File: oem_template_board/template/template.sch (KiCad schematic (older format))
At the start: 28 parts, among them J1 CONN_02X03, U1 MCP2561-E_SN, U101 TPS560430YF, U2 ATMEGA16M1, Y1 Crystal_SMD

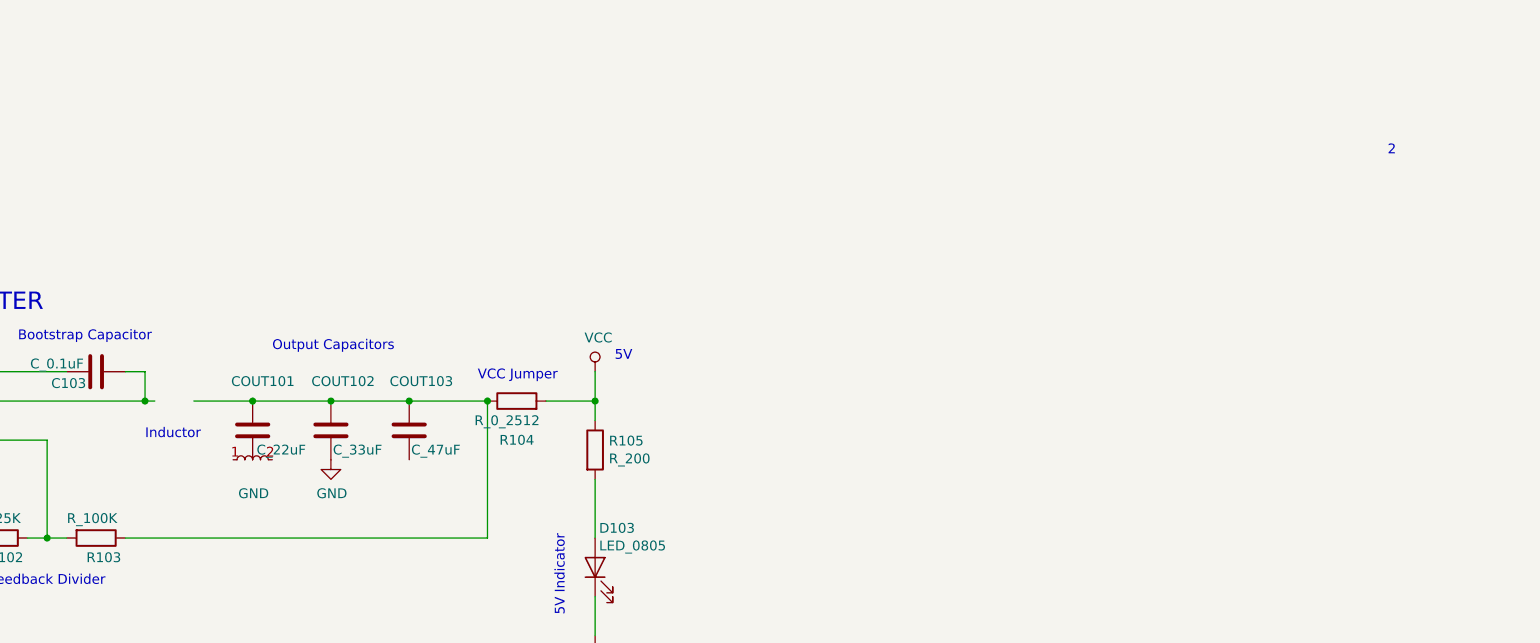
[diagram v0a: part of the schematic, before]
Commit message: fix inductor and bypass cap connections
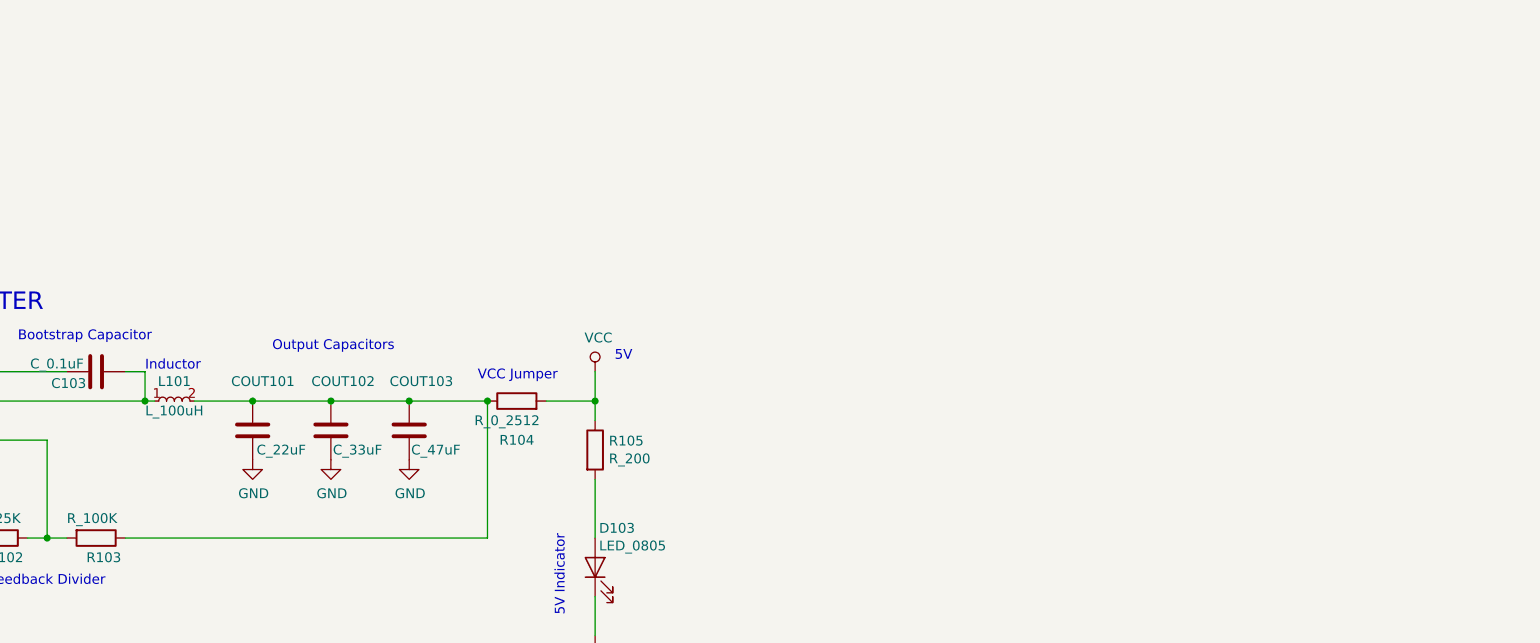
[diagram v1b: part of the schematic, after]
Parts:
- added L101: L_100uH, formula:L_100uH, symbol template-rescue:L_100uH-formula
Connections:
- net GND: now also COUT101.2, COUT103.2
- net at C103.2, U101.6 (SW): now also L101.1
- net at COUT101.1, COUT102.1, COUT103.1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: now also L101.2
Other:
- note removed: "2"
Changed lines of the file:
@@
 Text Notes 3450 9850 0    50   ~ 0
 Feedback Divider\n
-Text Notes 4250 9100 0    50   ~ 0
-Inductor\n
 Text Notes 3600 8600 0    50   ~ 0
 Bootstrap Capacitor\n
 Text Notes 4900 8650 0    50   ~ 0
 Output Capacitors\n
-$Comp
-L template-rescue:L_100uH-formula #PWR0109
-U 1 1 5C781579
-P 4800 9200
-F 0 "#PWR0109" H 4800 8950 50  0001 C CNN
-F 1 "GND" H 4805 9027 50  0000 C CNN
-F 2 "" H 4800 9200 50  0001 C CNN
-F 3 "" H 4800 9200 50  0001 C CNN
-F 4 "Digikey" H 4900 9000 50  0001 C CNN "MFN"
-F 5 "445-15759-1-ND" H 4800 9450 50  0001 C CNN "MPN"
-F 6 "https://www.digikey.com/product-detail/en/tdk-corporation/NLFV32T-101K-EF/445-15759-1-ND/4328055" H 5100 9400 50  0001 C CNN "Link"
-	1    4800 9200
-	1    0    0    -1
-$EndComp
 $Comp
 L power:GND #PWR0110
@@
 Text Notes 6400 10000 1    50   ~ 0
 5V Indicator
-Text Notes 10600 7650 0    50   ~ 0
-2
 $Comp
 L template-rescue:ATMEGA16M1-formula U2
@@
 	1700 8800 2100 8800
 Connection ~ 1700 8800
+Text Notes 4250 8750 0    50   ~ 0
+Inductor\n
+$Comp
+L power:GND #PWR?
+U 1 1 5F87F709
+P 4800 9200
+F 0 "#PWR?" H 4800 8950 50  0001 C CNN
+F 1 "GND" H 4805 9027 50  0000 C CNN
+F 2 "" H 4800 9200 50  0001 C CNN
+F 3 "" H 4800 9200 50  0001 C CNN
+	1    4800 9200
+	1    0    0    -1
+$EndComp
+$Comp
+L power:GND #PWR?
+U 1 1 5F87F995
+P 5600 9200
+F 0 "#PWR?" H 5600 8950 50  0001 C CNN
+F 1 "GND" H 5605 9027 50  0000 C CNN
+F 2 "" H 5600 9200 50  0001 C CNN
+F 3 "" H 5600 9200 50  0001 C CNN
+	1    5600 9200
+	1    0    0    -1
+$EndComp
+$Comp
+L template-rescue:L_100uH-formula L101
+U 1 1 5F881F17
+P 4400 8900
+F 0 "L101" H 4400 9000 50  0000 C CNN
+F 1 "L_100uH" H 4400 8850 50  0000 C CNN
+F 2 "formula:L_100uH" H 4300 8700 50  0001 C CNN
+F 3 "https://product.tdk.com/info/en/catalog/datasheets/inductor_commercial_decoupling_nlfv32-ef_en.pdf" H 4300 8750 50  0001 C CNN
+F 4 "Digikey" H 4500 8700 50  0001 C CNN "MFN"
+F 5 "445-15759-1-ND" H 4400 9150 50  0001 C CNN "MPN"
+F 6 "https://www.digikey.com/product-detail/en/tdk-corporation/NLFV32T-101K-EF/445-15759-1-ND/4328055" H 4700 9100 50  0001 C CNN "Link"
+	1    4400 8900
+	1    0    0    -1
+$EndComp
 $EndSCHEMATC

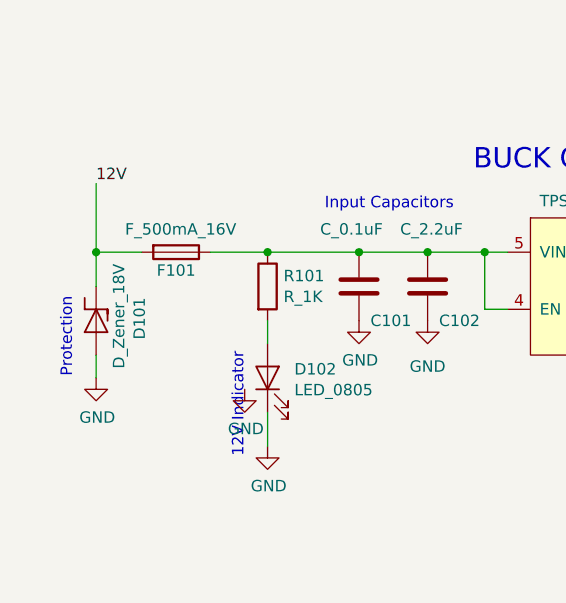
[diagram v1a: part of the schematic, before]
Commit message: move fuse before zener diode so it pops during an over-voltage event
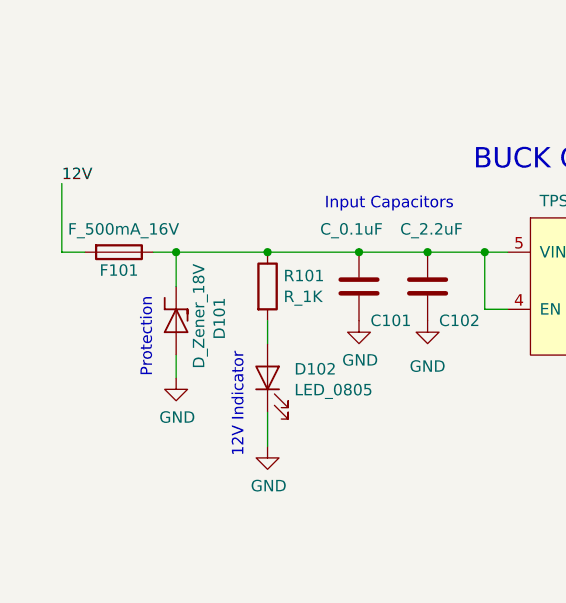
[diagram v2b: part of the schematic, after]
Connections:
- net 12V: no longer D101.1 (K)
- net at C101.1, C102.1, F101.1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: now also D101.1 (K)
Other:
- moved on the sheet: D101, F101
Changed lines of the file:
@@
 L template-rescue:F_500mA_16V-formula F101
 U 1 1 5C0BFA29
-P 1300 8800
-F 0 "F101" V 1380 8800 50  0000 C CNN
-F 1 "F_500mA_16V" V 1200 8820 50  0000 C CNN
-F 2 "footprints:Fuse_1210" V 1230 8800 50  0001 C CNN
-F 3 "https://belfuse.com/resources/CircuitProtection/datasheets/0ZCH%20Nov2016.pdf" V 1380 8800 50  0001 C CNN
-F 4 "DK" H 1300 8800 60  0001 C CNN "MFN"
-F 5 "507-1786-1-ND" H 1300 8800 60  0001 C CNN "MPN"
-F 6 "https://www.digikey.com/product-detail/en/bel-fuse-inc/0ZCH0050FF2G/507-1786-1-ND/4156209" V 1780 9200 60  0001 C CNN "PurchasingLink"
-	1    1300 8800
+P 1050 8800
+F 0 "F101" V 1130 8800 50  0000 C CNN
+F 1 "F_500mA_16V" V 950 8820 50  0000 C CNN
+F 2 "footprints:Fuse_1210" V 980 8800 50  0001 C CNN
+F 3 "https://belfuse.com/resources/CircuitProtection/datasheets/0ZCH%20Nov2016.pdf" V 1130 8800 50  0001 C CNN
+F 4 "DK" H 1050 8800 60  0001 C CNN "MFN"
+F 5 "507-1786-1-ND" H 1050 8800 60  0001 C CNN "MPN"
+F 6 "https://www.digikey.com/product-detail/en/bel-fuse-inc/0ZCH0050FF2G/507-1786-1-ND/4156209" V 1530 9200 60  0001 C CNN "PurchasingLink"
+	1    1050 8800
 	0    1    1    0
 $EndComp
@@
 L template-rescue:D_Zener_18V-formula D101
 U 1 1 5C623D49
-P 950 9100
-F 0 "D101" H 940 9290 50  0000 C CNN
-F 1 "D_Zener_18V" H 930 9200 50  0000 C CNN
-F 2 "footprints:DO-214AA" H 850 9100 50  0001 C CNN
-F 3 "http://www.mccsemi.com/up_pdf/SMBJ5338B-SMBJ5388B(SMB).pdf" H 950 9200 50  0001 C CNN
-F 4 "DK" H 1150 9400 60  0001 C CNN "MFN"
-F 5 "SMBJ5355B-TPMSCT-ND" H 1050 9300 60  0001 C CNN "MPN"
-F 6 "https://www.digikey.com/products/en?keywords=SMBJ5355B-TPMSCT-ND" H 1350 9600 60  0001 C CNN "PurchasingLink"
-	1    950  9100
+P 1300 9100
+F 0 "D101" H 1290 9290 50  0000 C CNN
+F 1 "D_Zener_18V" H 1280 9200 50  0000 C CNN
+F 2 "footprints:DO-214AA" H 1200 9100 50  0001 C CNN
+F 3 "http://www.mccsemi.com/up_pdf/SMBJ5338B-SMBJ5388B(SMB).pdf" H 1300 9200 50  0001 C CNN
+F 4 "DK" H 1500 9400 60  0001 C CNN "MFN"
+F 5 "SMBJ5355B-TPMSCT-ND" H 1400 9300 60  0001 C CNN "MPN"
+F 6 "https://www.digikey.com/products/en?keywords=SMBJ5355B-TPMSCT-ND" H 1700 9600 60  0001 C CNN "PurchasingLink"
+	1    1300 9100
 	0    1    1    0
 $EndComp
@@
 L power:GND #PWR0101
 U 1 1 5C62BB38
-P 950 9350
-F 0 "#PWR0101" H 950 9100 50  0001 C CNN
-F 1 "GND" H 955 9177 50  0000 C CNN
-F 2 "" H 950 9350 50  0001 C CNN
-F 3 "" H 950 9350 50  0001 C CNN
-	1    950  9350
-	1    0    0    -1
-$EndComp
-Text Label 950  8500 0    50   ~ 0
+P 1300 9350
+F 0 "#PWR0101" H 1300 9100 50  0001 C CNN
+F 1 "GND" H 1305 9177 50  0000 C CNN
+F 2 "" H 1300 9350 50  0001 C CNN
+F 3 "" H 1300 9350 50  0001 C CNN
+	1    1300 9350
+	1    0    0    -1
+$EndComp
+Text Label 800  8500 0    50   ~ 0
 12V
 $Comp
@@
 Text Notes 1600 9700 1    50   ~ 0
 12V Indicator
-Text Notes 850  9350 1    50   ~ 0
+Text Notes 1200 9350 1    50   ~ 0
 Protection\n
 Text Notes 2600 8450 0    89   ~ 0
@@
 F 3 "" H 5200 9200 50  0001 C CNN
 	1    5200 9200
-	1    0    0    -1
-$EndComp
-$Comp
-L power:GND #PWR0111
-U 1 1 5C781DA3
-P 1600 9400
-F 0 "#PWR0111" H 1600 9150 50  0001 C CNN
-F 1 "GND" H 1605 9227 50  0000 C CNN
-F 2 "" H 1600 9400 50  0001 C CNN
-F 3 "" H 1600 9400 50  0001 C CNN
-	1    1600 9400
 	1    0    0    -1
 $EndComp
@@
 	6550 9300 6550 9600
 Wire Wire Line
-	950  9250 950  9350
-Wire Wire Line
-	950  8800 1150 8800
-Connection ~ 950  8800
+	1300 9250 1300 9350
 Connection ~ 2100 8800
 Wire Wire Line
@@
 	15300 2150 15400 2150
 Wire Wire Line
-	950  8800 950  8950
-Wire Wire Line
-	950  8500 950  8800
+	800  8500 800  8800
 $Comp
 L template-rescue:TPS560430YF-formula U101
@@
 $EndComp
 Wire Wire Line
-	1450 8800 1700 8800
-Wire Wire Line
 	1700 8800 2100 8800
 Connection ~ 1700 8800
@@
 	1    0    0    -1
 $EndComp
+Wire Wire Line
+	800  8800 900  8800
+Wire Wire Line
+	1200 8800 1300 8800
+Wire Wire Line
+	1300 8950 1300 8800
+Connection ~ 1300 8800
+Wire Wire Line
+	1300 8800 1700 8800
 $EndSCHEMATC

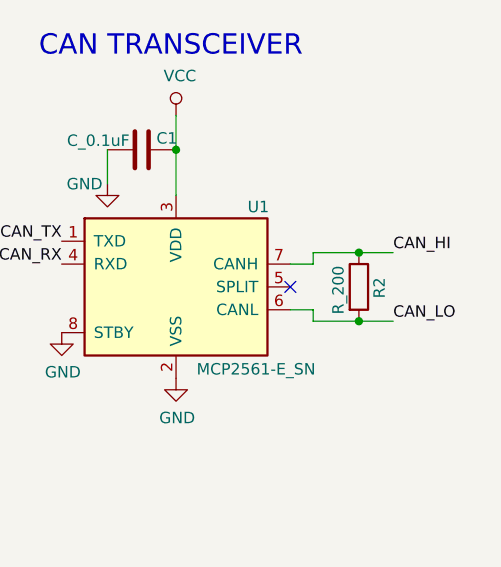
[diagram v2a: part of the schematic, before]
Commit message: switch terminating resistor on can transceiver to 120_DNP
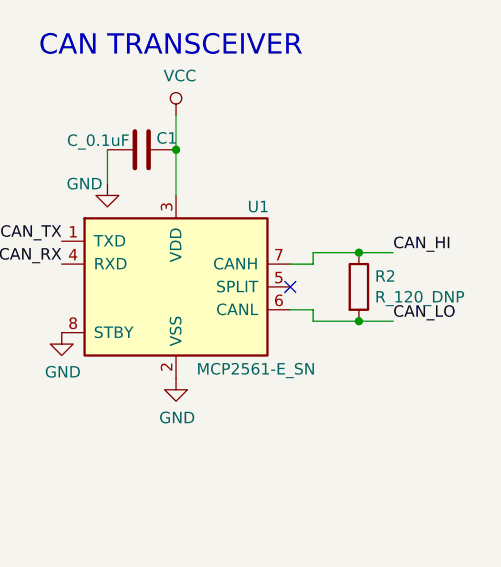
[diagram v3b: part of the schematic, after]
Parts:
- removed R2: R_200, footprints:R_0805_OEM, symbol template-rescue:R_200-formula
- added R2: R_120_DNP, footprints:R_0805_OEM, symbol formula:R_120_DNP
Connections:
- net CAN_HI: now also R2.1
- net CAN_LO: now also R2.2
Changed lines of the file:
@@
 	0    1    1    0
-$EndComp
-$Comp
-L template-rescue:R_200-formula R2
-U 1 1 5D5FB79E
-P 15600 2050
-F 0 "R2" V 15690 2000 50  0000 L CNN
-F 1 "R_200" V 15510 1930 50  0000 L CNN
-F 2 "footprints:R_0805_OEM" H 15530 2050 50  0001 C CNN
-F 3 "https://www.seielect.com/Catalog/SEI-RMCF_RMCP.pdf" H 15680 2050 50  0001 C CNN
-F 4 "DK" H 15600 2050 60  0001 C CNN "MFN"
-F 5 "RMCF0805JT200RCT-ND" H 15600 2050 60  0001 C CNN "MPN"
-F 6 "https://www.digikey.com/products/en?keywords=RMCF0805JT200RCT-ND" H 16080 2450 60  0001 C CNN "PurchasingLink"
-	1    15600 2050
-	1    0    0    -1
 $EndComp
 NoConn ~ 15300 2050
@@
 	15400 1950 15400 1900
 Wire Wire Line
-	15400 1900 15600 1900
-Connection ~ 15600 1900
-Wire Wire Line
-	15600 1900 15750 1900
-Wire Wire Line
 	15400 2150 15400 2200
-Wire Wire Line
-	15400 2200 15600 2200
-Connection ~ 15600 2200
-Wire Wire Line
-	15600 2200 15750 2200
 Wire Wire Line
 	14250 8450 14250 8600
@@
 Wire Wire Line
 	1300 8800 1700 8800
+$Comp
+L formula:R_120_DNP R2
+U 1 1 5FA5AB4A
+P 15600 2050
+F 0 "R2" H 15670 2096 50  0000 L CNN
+F 1 "R_120_DNP" H 15670 2005 50  0000 L CNN
+F 2 "footprints:R_0805_OEM" H 14400 2200 50  0001 L CNN
+F 3 "https://www.mouser.com/datasheet/2/315/AOA0000C304-1149620.pdf" H 14400 2500 50  0001 L CNN
+F 4 "DK" H 15600 2050 60  0001 C CNN "MFN"
+F 5 "667-ERJ-6ENF1200V" H 14400 2300 60  0001 L CNN "MPN"
+F 6 "https://www.mouser.com/ProductDetail/Panasonic-Industrial-Devices/ERJ-6ENF1200V?qs=sGAEpiMZZMvdGkrng054t8AJgcdMkx7x%252bFQnctTMUmU%3d" H 14400 2400 60  0001 L CNN "PurchasingLink"
+	1    15600 2050
+	1    0    0    -1
+$EndComp
+Wire Wire Line
+	15400 1900 15600 1900
+Wire Wire Line
+	15400 2200 15600 2200
+Connection ~ 15600 1900
+Wire Wire Line
+	15600 1900 15750 1900
+Connection ~ 15600 2200
+Wire Wire Line
+	15600 2200 15750 2200
 $EndSCHEMATC
